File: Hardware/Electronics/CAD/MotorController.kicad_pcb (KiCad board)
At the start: 2 copper layers, 42.3 x 42.3 mm, 16 parts, among them J1 MPE 094-1-006, J2 CONN_01X03, J3 Screw_Terminal_1x02, J5 CONN_01X04, SW2 SW_DPST_x2, U1 LD1117S33CTR, U2 MAX471, U3 TMC2130, U4 ESP-12E, U5 HiLink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

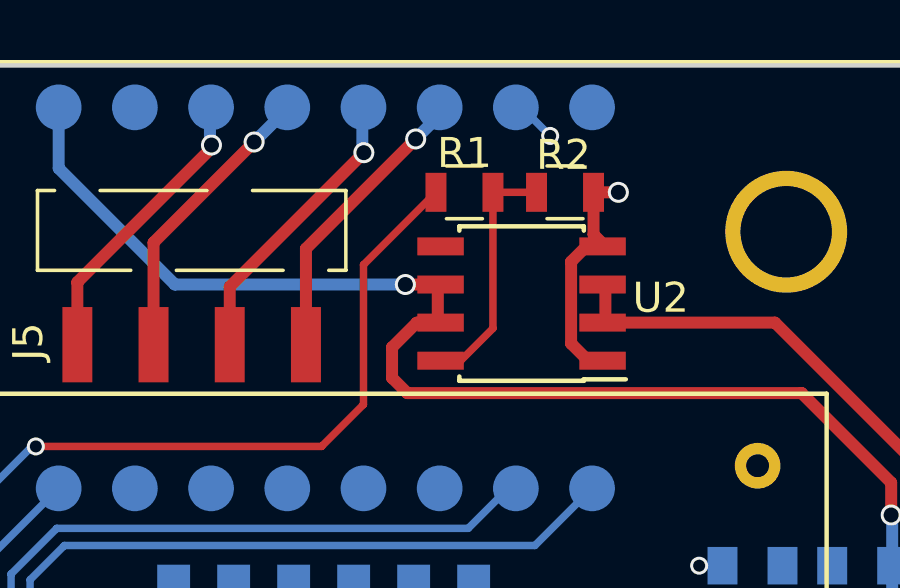
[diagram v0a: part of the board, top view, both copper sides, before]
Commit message: bug fix current sensor
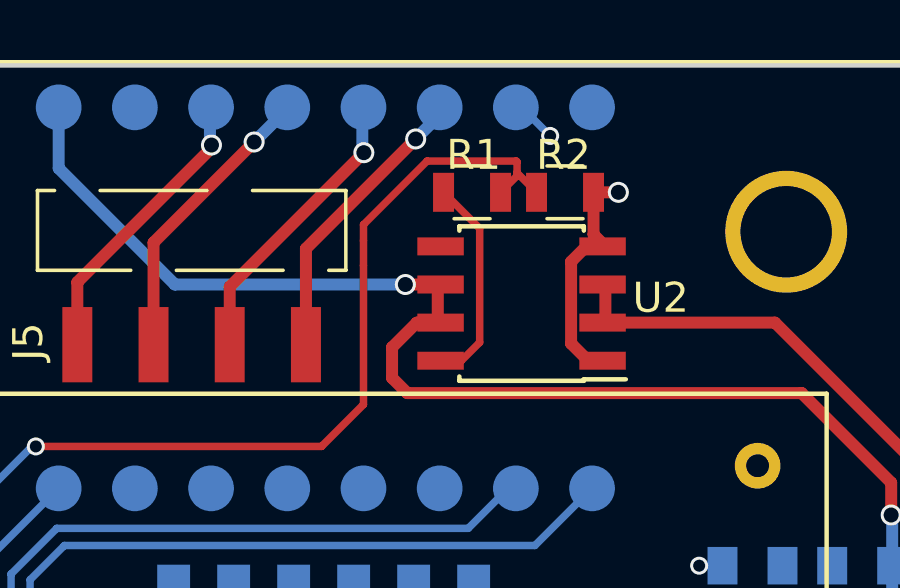
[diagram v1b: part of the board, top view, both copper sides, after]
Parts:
- J3: value Screw_Terminal_1x02 -> SolderTerminal
- R1: value RND 0805 1 10K -> RND 0805 1 47K
- R2: value RND 0805 1 10K -> RND 0805 1 100K
- SW2: value SW_DPST_x2 -> Taster 9314
- moved R1 0.25 mm to (202.2, 41.5), turned to 180 degrees
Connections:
- R2 pad 2: Net-(R1-Pad2) -> CURRENT_FEEDBACK
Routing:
- net CURRENT_FEEDBACK: track 42.4 -> 48.5 mm
- net Net-(R1-Pad2): track 8.39 -> 7.82 mm
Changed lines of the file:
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@@
     (thickness 1.6)
     (drawings 5)
-    (tracks 168)
+    (tracks 176)
     (zones 0)
     (modules 16)
@@
       (effects (font (size 1 1) (thickness 0.15)))
     )
-    (fp_text value SW_DPST_x2 (at 0 3.7 270) (layer F.Fab)
+    (fp_text value "Taster 9314" (at 0 3.7 270) (layer F.Fab)
       (effects (font (size 1 1) (thickness 0.15)))
     )
@@
       (effects (font (size 1 1) (thickness 0.15)) (justify mirror))
     )
-    (fp_text value Screw_Terminal_1x02 (at 0 -6.14) (layer B.Fab)
+    (fp_text value SolderTerminal (at 0 -6.14) (layer B.Fab)
       (effects (font (size 1 1) (thickness 0.15)) (justify mirror))
     )
@@
   )
   (module Resistors_SMD:R_0805 (layer F.Cu)
-    (at 201.93 41.5036)
+    (at 202.184 41.5036 180)
     (descr "Resistor SMD 0805, reflow soldering, Vishay (see dcrcw.pdf)")
     (tags "resistor 0805")
     (attr smd)
-    (fp_text reference R1 (at 0 -1.3081) (layer F.SilkS)
-      (effects (font (size 1 1) (thickness 0.15)))
-    )
-    (fp_text value "RND 0805 1 10K" (at 0 1.75) (layer F.Fab)
-      (effects (font (size 1 1) (thickness 0.15)))
-    )
-    (fp_text user %R (at 0 0) (layer F.Fab)
-      (effects (font (size 0.5 0.5) (thickness 0.075)))
-    )
-    (fp_line (start -1 0.62) (end -1 -0.62) (layer F.Fab) (width 0.1))
-    (fp_line (start 1 0.62) (end -1 0.62) (layer F.Fab) (width 0.1))
-    (fp_line (start 1 -0.62) (end 1 0.62) (layer F.Fab) (width 0.1))
-    (fp_line (start -1 -0.62) (end 1 -0.62) (layer F.Fab) (width 0.1))
-    (fp_line (start 0.6 0.88) (end -0.6 0.88) (layer F.SilkS) (width 0.12))
-    (fp_line (start -0.6 -0.88) (end 0.6 -0.88) (layer F.SilkS) (width 0.12))
-    (fp_line (start -1.55 -0.9) (end 1.55 -0.9) (layer F.CrtYd) (width 0.05))
-    (fp_line (start -1.55 -0.9) (end -1.55 0.9) (layer F.CrtYd) (width 0.05))
-    (fp_line (start 1.55 0.9) (end 1.55 -0.9) (layer F.CrtYd) (width 0.05))
-    (fp_line (start 1.55 0.9) (end -1.55 0.9) (layer F.CrtYd) (width 0.05))
-    (pad 1 smd rect (at -0.95 0) (size 0.7 1.3) (layers F.Cu F.Paste F.Mask)
-      (net 26 CURRENT_FEEDBACK))
-    (pad 2 smd rect (at 0.95 0) (size 0.7 1.3) (layers F.Cu F.Paste F.Mask)
-      (net 36 "Net-(R1-Pad2)"))
-    (model ${KISYS3DMOD}/Resistors_SMD.3dshapes/R_0805.wrl
-      (at (xyz 0 0 0))
-      (scale (xyz 1 1 1))
-      (rotate (xyz 0 0 0))
-    )
-  )
-  (module Resistors_SMD:R_0805 (layer F.Cu)
-    (at 205.2828 41.5036 180)
-    (descr "Resistor SMD 0805, reflow soldering, Vishay (see dcrcw.pdf)")
-    (tags "resistor 0805")
-    (attr smd)
-    (fp_text reference R2 (at 0.0508 1.2446 180) (layer F.SilkS)
-      (effects (font (size 1 1) (thickness 0.15)))
-    )
-    (fp_text value "RND 0805 1 10K" (at 0 1.75 180) (layer F.Fab)
+    (fp_text reference R1 (at -0.0508 1.2446 180) (layer F.SilkS)
+      (effects (font (size 1 1) (thickness 0.15)))
+    )
+    (fp_text value "RND 0805 1 47K" (at 0 1.75 180) (layer F.Fab)
       (effects (font (size 1 1) (thickness 0.15)))
     )
@@
     (fp_line (start 1.55 0.9) (end -1.55 0.9) (layer F.CrtYd) (width 0.05))
     (pad 1 smd rect (at -0.95 0 180) (size 0.7 1.3) (layers F.Cu F.Paste F.Mask)
-      (net 1 GND))
+      (net 26 CURRENT_FEEDBACK))
     (pad 2 smd rect (at 0.95 0 180) (size 0.7 1.3) (layers F.Cu F.Paste F.Mask)
       (net 36 "Net-(R1-Pad2)"))
+    (model ${KISYS3DMOD}/Resistors_SMD.3dshapes/R_0805.wrl
+      (at (xyz 0 0 0))
+      (scale (xyz 1 1 1))
+      (rotate (xyz 0 0 0))
+    )
+  )
+  (module Resistors_SMD:R_0805 (layer F.Cu)
+    (at 205.2828 41.5036 180)
+    (descr "Resistor SMD 0805, reflow soldering, Vishay (see dcrcw.pdf)")
+    (tags "resistor 0805")
+    (attr smd)
+    (fp_text reference R2 (at 0.0508 1.2446 180) (layer F.SilkS)
+      (effects (font (size 1 1) (thickness 0.15)))
+    )
+    (fp_text value "RND 0805 1 100K" (at 0 1.75 180) (layer F.Fab)
+      (effects (font (size 1 1) (thickness 0.15)))
+    )
+    (fp_text user %R (at 0 0 180) (layer F.Fab)
+      (effects (font (size 0.5 0.5) (thickness 0.075)))
+    )
+    (fp_line (start -1 0.62) (end -1 -0.62) (layer F.Fab) (width 0.1))
+    (fp_line (start 1 0.62) (end -1 0.62) (layer F.Fab) (width 0.1))
+    (fp_line (start 1 -0.62) (end 1 0.62) (layer F.Fab) (width 0.1))
+    (fp_line (start -1 -0.62) (end 1 -0.62) (layer F.Fab) (width 0.1))
+    (fp_line (start 0.6 0.88) (end -0.6 0.88) (layer F.SilkS) (width 0.12))
+    (fp_line (start -0.6 -0.88) (end 0.6 -0.88) (layer F.SilkS) (width 0.12))
+    (fp_line (start -1.55 -0.9) (end 1.55 -0.9) (layer F.CrtYd) (width 0.05))
+    (fp_line (start -1.55 -0.9) (end -1.55 0.9) (layer F.CrtYd) (width 0.05))
+    (fp_line (start 1.55 0.9) (end 1.55 -0.9) (layer F.CrtYd) (width 0.05))
+    (fp_line (start 1.55 0.9) (end -1.55 0.9) (layer F.CrtYd) (width 0.05))
+    (pad 1 smd rect (at -0.95 0 180) (size 0.7 1.3) (layers F.Cu F.Paste F.Mask)
+      (net 1 GND))
+    (pad 2 smd rect (at 0.95 0 180) (size 0.7 1.3) (layers F.Cu F.Paste F.Mask)
+      (net 26 CURRENT_FEEDBACK))
     (model ${KISYS3DMOD}/Resistors_SMD.3dshapes/R_0805.wrl
       (at (xyz 0 0 0))
@@
   (segment (start 212.2805 45.847) (end 217.2335 50.8) (width 0.4) (layer F.Cu) (net 25))
   (segment (start 206.629 44.577) (end 206.629 45.847) (width 0.4) (layer F.Cu) (net 25))
+  (segment (start 203.6826 40.8534) (end 203.6826 40.955) (width 0.25) (layer F.Cu) (net 26))
+  (segment (start 203.6826 40.955) (end 203.134 41.5036) (width 0.25) (layer F.Cu) (net 26) (status 800000))
+  (segment (start 198.5645 43.1165) (end 198.5645 42.5831) (width 0.25) (layer F.Cu) (net 26))
+  (segment (start 203.6826 40.8534) (end 204.3328 41.5036) (width 0.25) (layer F.Cu) (net 26) (status 800000))
+  (segment (start 203.6826 40.4876) (end 203.6826 40.8534) (width 0.25) (layer F.Cu) (net 26))
+  (segment (start 203.6572 40.4622) (end 203.6826 40.4876) (width 0.25) (layer F.Cu) (net 26))
+  (segment (start 200.6854 40.4622) (end 203.6572 40.4622) (width 0.25) (layer F.Cu) (net 26))
+  (segment (start 198.5645 42.5831) (end 200.6854 40.4622) (width 0.25) (layer F.Cu) (net 26))
+  (segment (start 198.5645 43.942) (end 198.5645 43.1165) (width 0.25) (layer F.Cu) (net 26))
   (segment (start 190.246 68.866) (end 188.754 68.866) (width 0.25) (layer B.Cu) (net 26))
   (segment (start 188.754 68.866) (end 186.944 67.056) (width 0.25) (layer B.Cu) (net 26))
@@
   (segment (start 187.6425 49.9745) (end 197.1675 49.9745) (width 0.25) (layer F.Cu) (net 26))
   (segment (start 197.1675 49.9745) (end 198.5645 48.5775) (width 0.25) (layer F.Cu) (net 26))
-  (segment (start 198.5645 48.5775) (end 198.5645 43.9191) (width 0.25) (layer F.Cu) (net 26))
-  (segment (start 198.5645 43.9191) (end 200.98 41.5036) (width 0.25) (layer F.Cu) (net 26))
-  (segment (start 200.98 41.5036) (end 200.98 41.6408) (width 0.25) (layer F.Cu) (net 26))
+  (segment (start 198.5645 48.5775) (end 198.5645 43.942) (width 0.25) (layer F.Cu) (net 26))
+  (segment (start 204.3328 41.5036) (end 204.3328 41.6204) (width 0.25) (layer F.Cu) (net 26))
+  (segment (start 201.135 47.117) (end 201.8284 47.117) (width 0.25) (layer F.Cu) (net 36) (status C00000))
+  (segment (start 201.8284 47.117) (end 202.438 46.5074) (width 0.25) (layer F.Cu) (net 36) (status 400000))
+  (segment (start 202.438 46.5074) (end 202.438 42.7076) (width 0.25) (layer F.Cu) (net 36))
+  (segment (start 202.438 42.7076) (end 201.234 41.5036) (width 0.25) (layer F.Cu) (net 36) (status 800000))
   (segment (start 201.041 47.117) (end 201.803 47.117) (width 0.25) (layer F.Cu) (net 36))
-  (segment (start 202.88 46.04) (end 202.88 41.5036) (width 0.25) (layer F.Cu) (net 36))
-  (segment (start 201.803 47.117) (end 202.88 46.04) (width 0.25) (layer F.Cu) (net 36))
-  (segment (start 202.88 41.5036) (end 204.3328 41.5036) (width 0.25) (layer F.Cu) (net 36))
-  (segment (start 204.3328 41.5036) (end 204.3328 41.6204) (width 0.25) (layer F.Cu) (net 36))
   (zone (net 2) (net_name +3V3) (layer F.Cu) (hatch edge 0.508)
     (connect_pads (clearance 0.508))

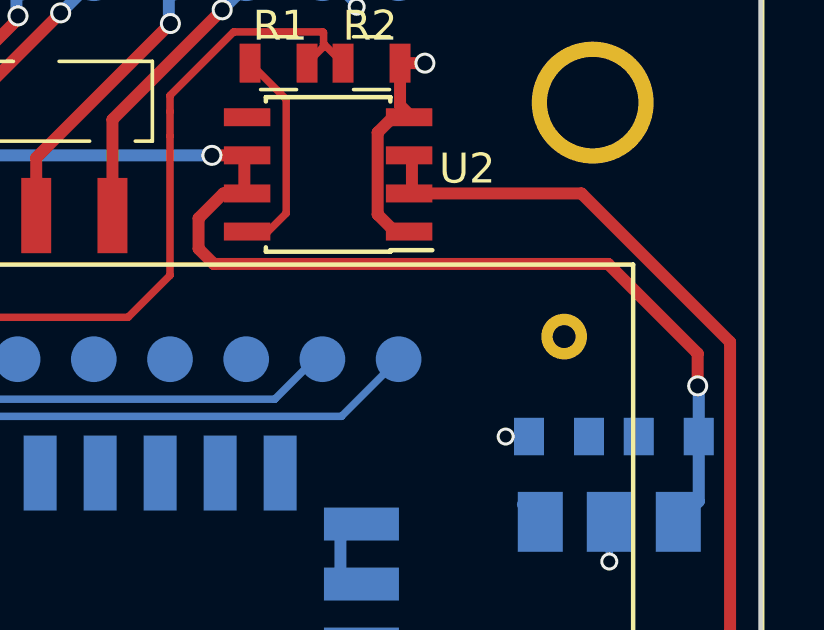
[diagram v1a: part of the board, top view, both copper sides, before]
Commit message: MAX741 missing resistor fix
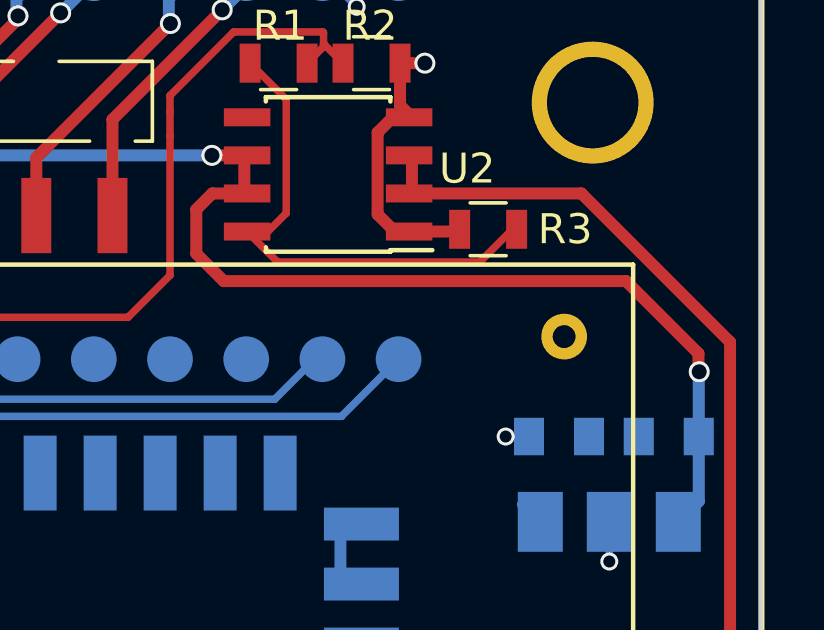
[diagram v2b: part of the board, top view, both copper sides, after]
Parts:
- added R3: RND 0805 1 2K, Resistors_SMD:R_0805, F.Cu at (209.2, 47.0)
- R1: value RND 0805 1 47K -> RND 0805 1 100K
- R2: value RND 0805 1 100K -> RND 0805 1 47K
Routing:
- net Net-(R1-Pad2): track 7.82 -> 17.7 mm
- net GND: track 15.1 -> 16.8 mm
- net +12V: track 44.6 -> 45.2 mm
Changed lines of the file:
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@@
 (kicad_pcb (version 4) (host pcbnew 4.0.6)
   (general
-    (links 54)
+    (links 56)
     (no_connects 1)
     (area 175.883499 37.199499 218.324501 79.640501)
     (thickness 1.6)
     (drawings 5)
-    (tracks 176)
+    (tracks 183)
     (zones 0)
-    (modules 16)
+    (modules 17)
     (nets 37)
   )
@@
     (tags "capacitor 0805")
     (attr smd)
-    (fp_text reference C1 (at 0 1.5) (layer B.SilkS)
+    (fp_text reference C1 (at 0.0508 -1.4224) (layer B.SilkS)
       (effects (font (size 1 1) (thickness 0.15)) (justify mirror))
     )
@@
     (tags "capacitor 0805")
     (attr smd)
-    (fp_text reference C2 (at 0 1.5) (layer B.SilkS)
+    (fp_text reference C2 (at -0.0254 -1.397) (layer B.SilkS)
       (effects (font (size 1 1) (thickness 0.15)) (justify mirror))
     )
@@
       (effects (font (size 1 1) (thickness 0.15)))
     )
-    (fp_text value "RND 0805 1 47K" (at 0 1.75 180) (layer F.Fab)
+    (fp_text value "RND 0805 1 100K" (at 0 1.75 180) (layer F.Fab)
       (effects (font (size 1 1) (thickness 0.15)))
     )
@@
       (effects (font (size 1 1) (thickness 0.15)))
     )
-    (fp_text value "RND 0805 1 100K" (at 0 1.75 180) (layer F.Fab)
+    (fp_text value "RND 0805 1 47K" (at 0 1.75 180) (layer F.Fab)
       (effects (font (size 1 1) (thickness 0.15)))
     )
@@
     )
   )
+  (module Resistors_SMD:R_0805 (layer F.Cu)
+    (at 209.169 47.0408)
+    (descr "Resistor SMD 0805, reflow soldering, Vishay (see dcrcw.pdf)")
+    (tags "resistor 0805")
+    (attr smd)
+    (fp_text reference R3 (at 2.5654 0) (layer F.SilkS)
+      (effects (font (size 1 1) (thickness 0.15)))
+    )
+    (fp_text value "RND 0805 1 2K" (at 0 1.75) (layer F.Fab)
+      (effects (font (size 1 1) (thickness 0.15)))
+    )
+    (fp_text user %R (at 0 0) (layer F.Fab)
+      (effects (font (size 0.5 0.5) (thickness 0.075)))
+    )
+    (fp_line (start -1 0.62) (end -1 -0.62) (layer F.Fab) (width 0.1))
+    (fp_line (start 1 0.62) (end -1 0.62) (layer F.Fab) (width 0.1))
+    (fp_line (start 1 -0.62) (end 1 0.62) (layer F.Fab) (width 0.1))
+    (fp_line (start -1 -0.62) (end 1 -0.62) (layer F.Fab) (width 0.1))
+    (fp_line (start 0.6 0.88) (end -0.6 0.88) (layer F.SilkS) (width 0.12))
+    (fp_line (start -0.6 -0.88) (end 0.6 -0.88) (layer F.SilkS) (width 0.12))
+    (fp_line (start -1.55 -0.9) (end 1.55 -0.9) (layer F.CrtYd) (width 0.05))
+    (fp_line (start -1.55 -0.9) (end -1.55 0.9) (layer F.CrtYd) (width 0.05))
+    (fp_line (start 1.55 0.9) (end 1.55 -0.9) (layer F.CrtYd) (width 0.05))
+    (fp_line (start 1.55 0.9) (end -1.55 0.9) (layer F.CrtYd) (width 0.05))
+    (pad 1 smd rect (at -0.95 0) (size 0.7 1.3) (layers F.Cu F.Paste F.Mask)
+      (net 1 GND))
+    (pad 2 smd rect (at 0.95 0) (size 0.7 1.3) (layers F.Cu F.Paste F.Mask)
+      (net 36 "Net-(R1-Pad2)"))
+    (model ${KISYS3DMOD}/Resistors_SMD.3dshapes/R_0805.wrl
+      (at (xyz 0 0 0))
+      (scale (xyz 1 1 1))
+      (rotate (xyz 0 0 0))
+    )
+  )
   (gr_line (start 218.2495 37.2745) (end 175.9585 37.2745) (angle 90) (layer Edge.Cuts) (width 0.15))
   (gr_line (start 218.2495 79.5655) (end 218.2495 37.2745) (angle 90) (layer Edge.Cuts) (width 0.15))
@@
     (effects (font (size 0.8 0.8) (thickness 0.125)) (justify left mirror))
   )
+  (segment (start 206.535 47.117) (end 208.1428 47.117) (width 0.4) (layer F.Cu) (net 1))
+  (segment (start 208.1428 47.117) (end 208.219 47.0408) (width 0.4) (layer F.Cu) (net 1))
   (segment (start 206.2328 41.5036) (end 206.2328 42.9108) (width 0.4) (layer F.Cu) (net 1))
   (segment (start 206.2328 42.9108) (end 206.629 43.307) (width 0.4) (layer F.Cu) (net 1))
@@
   (segment (start 199.1574 78.1598) (end 199.136 78.1812) (width 0.4) (layer F.Cu) (net 1))
   (segment (start 210.328 56.2144) (end 210.9076 56.794) (width 0.4) (layer B.Cu) (net 1))
+  (via (at 204.7875 39.624) (size 0.6) (drill 0.4) (layers F.Cu B.Cu) (net 2))
   (segment (start 203.6445 38.6715) (end 203.835 38.6715) (width 0.25) (layer B.Cu) (net 2))
   (segment (start 203.835 38.6715) (end 204.7875 39.624) (width 0.25) (layer B.Cu) (net 2))
-  (via (at 204.7875 39.624) (size 0.6) (drill 0.4) (layers F.Cu B.Cu) (net 2))
   (segment (start 190.246 56.866) (end 190.246 55.4736) (width 0.25) (layer B.Cu) (net 2))
   (via (at 190.246 55.4736) (size 0.6) (drill 0.4) (layers F.Cu B.Cu) (net 2))
@@
   (segment (start 210.5312 53.9496) (end 210.7692 53.9496) (width 0.25) (layer B.Cu) (net 2))
   (segment (start 213.2076 56.388) (end 213.2076 56.794) (width 0.25) (layer B.Cu) (net 2))
+  (segment (start 216.1888 53.9496) (end 216.1888 51.8066) (width 0.4) (layer B.Cu) (net 3))
+  (segment (start 199.9742 45.847) (end 201.135 45.847) (width 0.4) (layer F.Cu) (net 3))
+  (segment (start 199.4408 46.3804) (end 199.9742 45.847) (width 0.4) (layer F.Cu) (net 3))
+  (segment (start 199.4408 47.8536) (end 199.4408 46.3804) (width 0.4) (layer F.Cu) (net 3))
+  (segment (start 200.3552 48.768) (end 199.4408 47.8536) (width 0.4) (layer F.Cu) (net 3))
+  (segment (start 213.7664 48.768) (end 200.3552 48.768) (width 0.4) (layer F.Cu) (net 3))
+  (segment (start 216.1794 51.181) (end 213.7664 48.768) (width 0.4) (layer F.Cu) (net 3))
+  (segment (start 216.1794 51.7652) (end 216.1794 51.181) (width 0.4) (layer F.Cu) (net 3))
+  (segment (start 216.2048 51.7906) (end 216.1794 51.7652) (width 0.4) (layer F.Cu) (net 3))
+  (via (at 216.2048 51.7906) (size 0.7) (drill 0.5) (layers F.Cu B.Cu) (net 3))
+  (segment (start 216.1888 51.8066) (end 216.2048 51.7906) (width 0.4) (layer B.Cu) (net 3))
   (segment (start 188.4045 38.6715) (end 188.4045 40.7035) (width 0.4) (layer B.Cu) (net 3))
   (segment (start 199.9615 44.577) (end 201.041 44.577) (width 0.4) (layer F.Cu) (net 3))
@@
   (segment (start 192.278 44.577) (end 199.9615 44.577) (width 0.4) (layer B.Cu) (net 3))
   (segment (start 188.4045 40.7035) (end 192.278 44.577) (width 0.4) (layer B.Cu) (net 3))
-  (via (at 216.154 52.2605) (size 0.7) (drill 0.5) (layers F.Cu B.Cu) (net 3))
-  (segment (start 200.3425 45.847) (end 199.517 46.6725) (width 0.4) (layer F.Cu) (net 3))
-  (segment (start 199.517 46.6725) (end 199.517 47.6885) (width 0.4) (layer F.Cu) (net 3))
-  (segment (start 199.517 47.6885) (end 200.025 48.1965) (width 0.4) (layer F.Cu) (net 3))
-  (segment (start 200.025 48.1965) (end 213.1695 48.1965) (width 0.4) (layer F.Cu) (net 3))
-  (segment (start 213.1695 48.1965) (end 216.154 51.181) (width 0.4) (layer F.Cu) (net 3))
-  (segment (start 216.154 51.181) (end 216.154 52.2605) (width 0.4) (layer F.Cu) (net 3))
-  (segment (start 201.041 45.847) (end 200.3425 45.847) (width 0.4) (layer F.Cu) (net 3))
-  (segment (start 216.1888 52.2953) (end 216.1888 53.9496) (width 0.4) (layer B.Cu) (net 3))
-  (segment (start 216.154 52.2605) (end 216.1888 52.2953) (width 0.4) (layer B.Cu) (net 3))
   (segment (start 201.041 44.577) (end 201.041 45.847) (width 0.4) (layer F.Cu) (net 3))
   (segment (start 216.0524 53.8132) (end 216.1888 53.9496) (width 0.4) (layer B.Cu) (net 3))
@@
   (segment (start 206.629 44.577) (end 206.629 45.847) (width 0.4) (layer F.Cu) (net 25))
   (segment (start 203.6826 40.8534) (end 203.6826 40.955) (width 0.25) (layer F.Cu) (net 26))
-  (segment (start 203.6826 40.955) (end 203.134 41.5036) (width 0.25) (layer F.Cu) (net 26) (status 800000))
+  (segment (start 203.6826 40.955) (end 203.134 41.5036) (width 0.25) (layer F.Cu) (net 26))
   (segment (start 198.5645 43.1165) (end 198.5645 42.5831) (width 0.25) (layer F.Cu) (net 26))
-  (segment (start 203.6826 40.8534) (end 204.3328 41.5036) (width 0.25) (layer F.Cu) (net 26) (status 800000))
+  (segment (start 203.6826 40.8534) (end 204.3328 41.5036) (width 0.25) (layer F.Cu) (net 26))
   (segment (start 203.6826 40.4876) (end 203.6826 40.8534) (width 0.25) (layer F.Cu) (net 26))
   (segment (start 203.6572 40.4622) (end 203.6826 40.4876) (width 0.25) (layer F.Cu) (net 26))
@@
   (segment (start 198.5645 48.5775) (end 198.5645 43.942) (width 0.25) (layer F.Cu) (net 26))
   (segment (start 204.3328 41.5036) (end 204.3328 41.6204) (width 0.25) (layer F.Cu) (net 26))
-  (segment (start 201.135 47.117) (end 201.8284 47.117) (width 0.25) (layer F.Cu) (net 36) (status C00000))
-  (segment (start 201.8284 47.117) (end 202.438 46.5074) (width 0.25) (layer F.Cu) (net 36) (status 400000))
+  (segment (start 210.119 47.0408) (end 209.9818 47.0408) (width 0.25) (layer F.Cu) (net 36))
+  (segment (start 209.9818 47.0408) (end 208.8896 48.133) (width 0.25) (layer F.Cu) (net 36))
+  (segment (start 208.8896 48.133) (end 202.151 48.133) (width 0.25) (layer F.Cu) (net 36))
+  (segment (start 202.151 48.133) (end 201.135 47.117) (width 0.25) (layer F.Cu) (net 36))
+  (segment (start 201.135 47.117) (end 201.8284 47.117) (width 0.25) (layer F.Cu) (net 36))
+  (segment (start 201.8284 47.117) (end 202.438 46.5074) (width 0.25) (layer F.Cu) (net 36))
   (segment (start 202.438 46.5074) (end 202.438 42.7076) (width 0.25) (layer F.Cu) (net 36))
-  (segment (start 202.438 42.7076) (end 201.234 41.5036) (width 0.25) (layer F.Cu) (net 36) (status 800000))
+  (segment (start 202.438 42.7076) (end 201.234 41.5036) (width 0.25) (layer F.Cu) (net 36))
   (segment (start 201.041 47.117) (end 201.803 47.117) (width 0.25) (layer F.Cu) (net 36))
   (zone (net 2) (net_name +3V3) (layer F.Cu) (hatch edge 0.508)
